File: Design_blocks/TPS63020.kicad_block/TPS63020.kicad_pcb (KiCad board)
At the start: 4 copper layers, 11 parts, among them U5 TPS63020DSJR

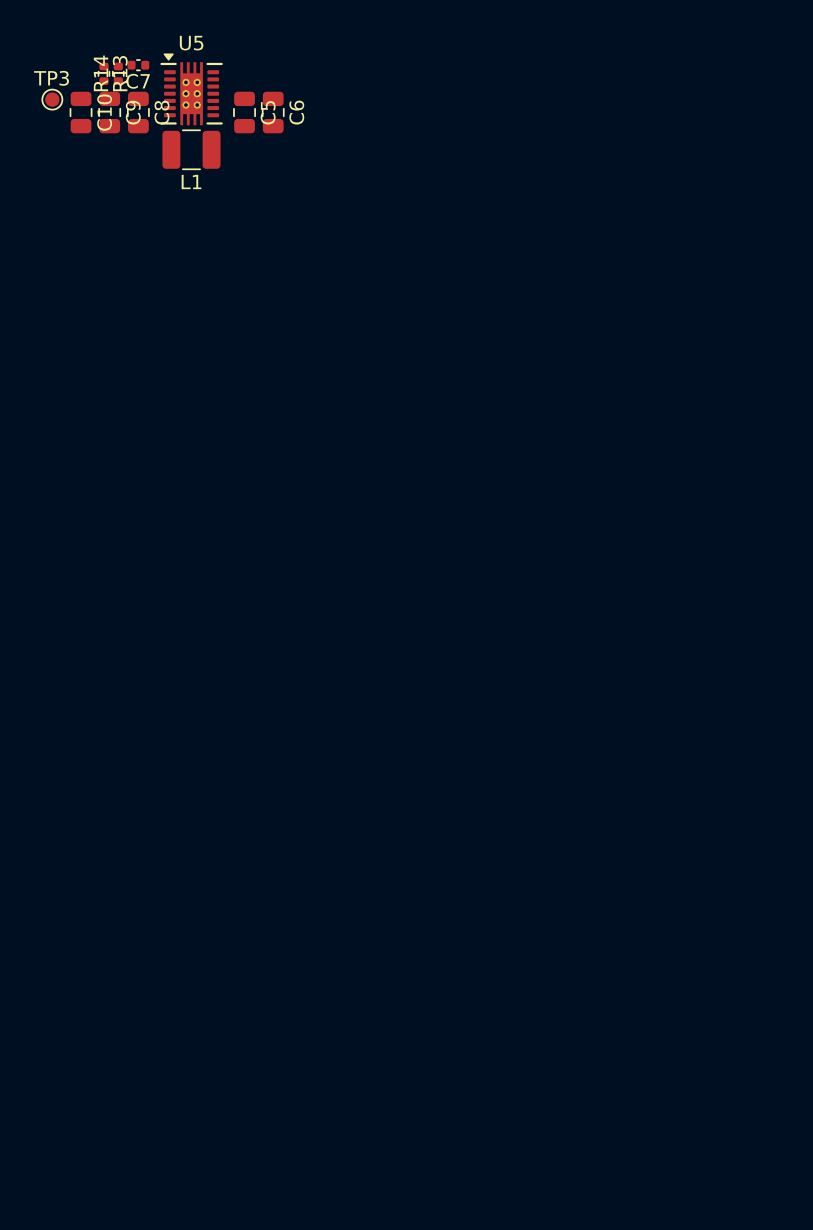
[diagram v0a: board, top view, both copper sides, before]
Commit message: Updated design block for tps63020
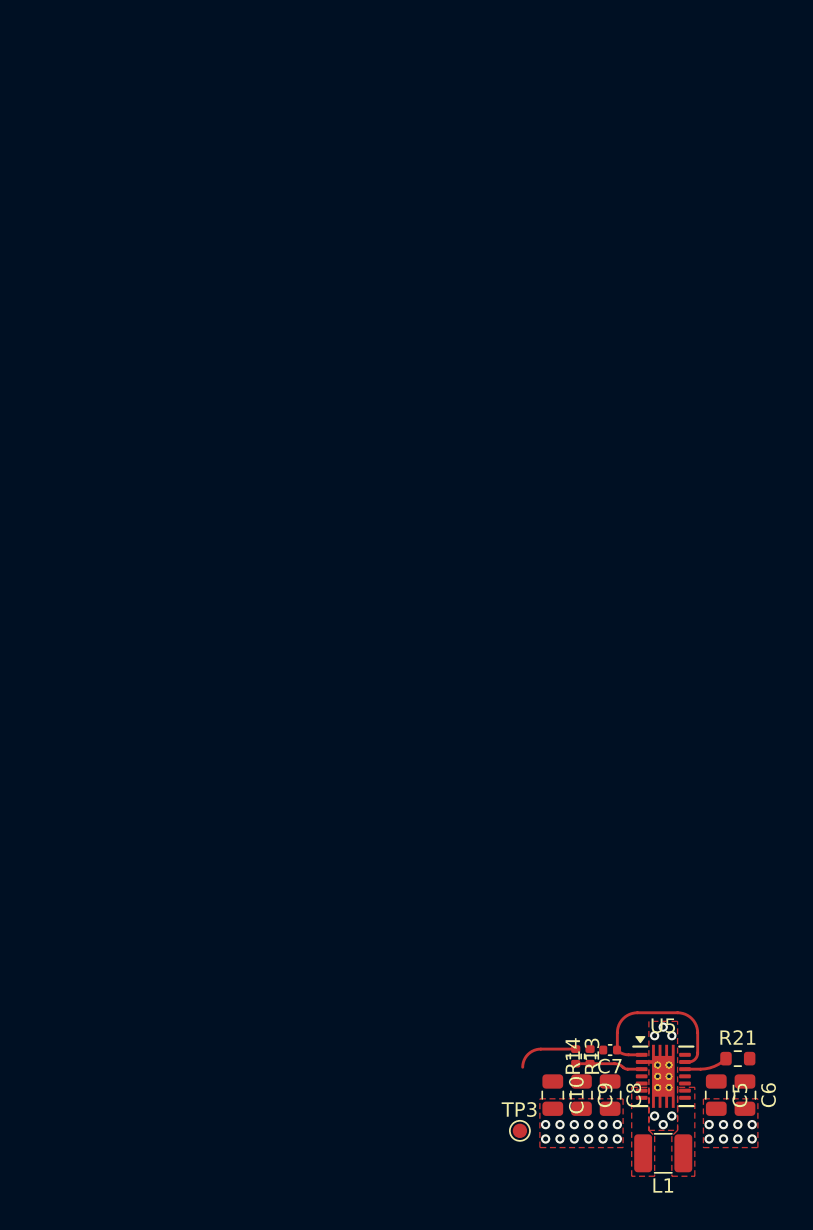
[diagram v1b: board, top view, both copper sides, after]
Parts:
- added R21: 10k, Resistor_SMD:R_0603_1608Metric, F.Cu at (170.8, 91.8)
- moved TP3 78.9 mm to (155.6, 96.8)
- moved L1 77.3 mm to (165.6, 98.4)
- moved C7 76.1 mm to (161.9, 91.2)
- moved C10 76.0 mm to (157.9, 94.3)
- moved C5 76.0 mm to (169.3, 94.3)
- moved C6 76.0 mm to (171.3, 94.3)
- moved C8 76.0 mm to (161.9, 94.3)
- moved C9 76.0 mm to (159.9, 94.3)
- moved R13 76.0 mm to (159.5, 91.6)
- moved R14 76.0 mm to (160.5, 91.6)
- moved U5 76.0 mm to (165.6, 93.0)
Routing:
- net Net-(U5-PS/SYNC): track 0.00 -> 12.7 mm
- net +3V3: track 0.00 -> 4.91 mm
- net Net-(U5-FB): track 0.00 -> 4.69 mm
- net /en: track 0.00 -> 3.11 mm
- net GND: track 0.00 -> 1.23 mm, vias 0 -> 26
- added copper zone on F.Cu, net GND
- added copper zone on F.Cu, net Net-(L1-Pad1)
- added copper zone on F.Cu, net Net-(L1-Pad2)
